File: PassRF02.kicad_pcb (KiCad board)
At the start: 2 copper layers, 70.5 x 33 mm, 4 parts, among them J1 PINHD_1x10_Male, J2 PINHD_1x10_Male, U1 WeMos_D1_mini, U2 ProMicro

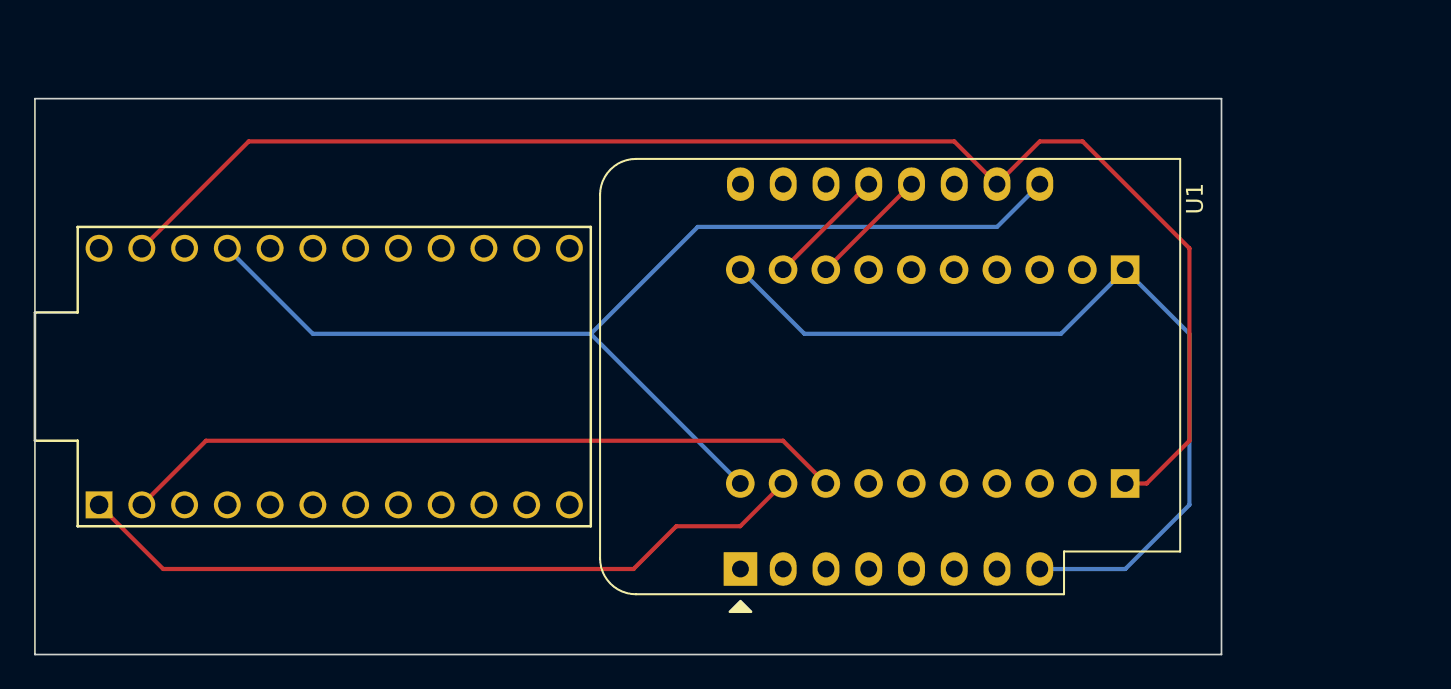
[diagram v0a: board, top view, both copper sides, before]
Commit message: Add reset button and killswitch
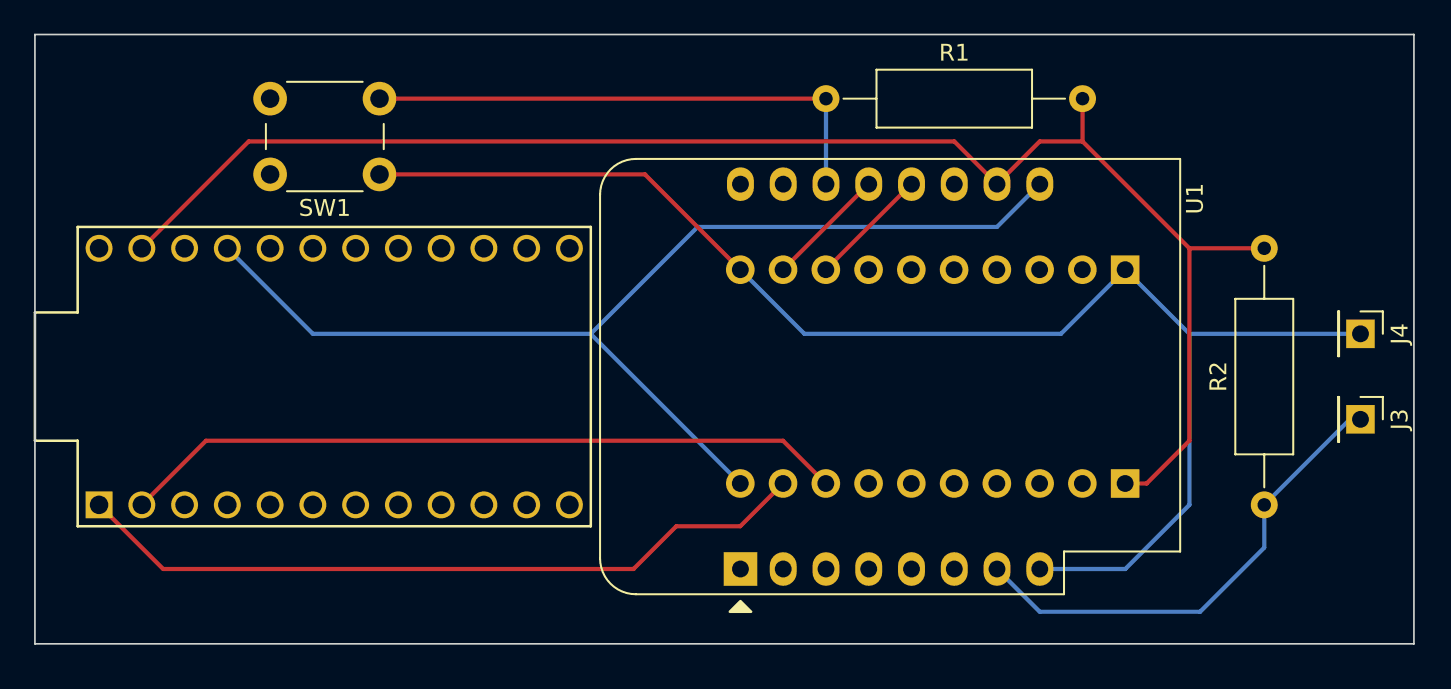
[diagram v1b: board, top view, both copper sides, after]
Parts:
- added J3: PINHD_1x1_Male, Connector_PinHeader_2.54mm:PinHeader_1x01_P2.54mm_Vertical, F.Cu at (195.6, 102.9)
- added J4: PINHD_1x1_Male, Connector_PinHeader_2.54mm:PinHeader_1x01_P2.54mm_Vertical, F.Cu at (195.6, 97.8)
- added R1: Resistor_0.5W, Resistor_THT:R_Axial_DIN0309_L9.0mm_D3.2mm_P15.24mm_Horizontal, F.Cu at (163.8, 83.8)
- added R2: Resistor_0.5W, Resistor_THT:R_Axial_DIN0309_L9.0mm_D3.2mm_P15.24mm_Horizontal, F.Cu at (189.9, 108.0)
- added SW1: Push_Button, Button_Switch_THT:SW_PUSH_6mm, F.Cu at (137.3, 88.3)
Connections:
- U1 pad 14: unconnected-(U1-SCL/D1-Pad14) -> Net-(U1-SCL/D1)
- U1 pad 7: unconnected-(U1-CS/D8-Pad7) -> Net-(U1-CS/D8)
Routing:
- net Net-(U1-3V3): track 52.0 -> 86.0 mm
- net Net-(U1-SCL/D1): track 0.00 -> 31.6 mm
- net Net-(U1-CS/D8): track 0.00 -> 28.9 mm
- net Net-(U1-GND): track 85.9 -> 92.9 mm
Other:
- board size 70.5 x 33 mm -> 81.9 x 36.2 mm
